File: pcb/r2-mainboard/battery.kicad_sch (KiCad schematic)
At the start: 38 parts, among them J1 USB-C 16P, J2 Pico-Lock 504050-0391, J25 SolderPads 3x, U1 BQ25892RTW, U2 MAX17048G+T10, U3 USBLC6-2SC6

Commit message: R2: the six approved edits, and one of them was already done
Owner-approved 2026-08-19, KiCad closed for the pass.

1. R225 22k -> 20.5K/1%, LCSC C57105 (0402WGF2052TCE, UNI-ROYAL, the
   family the rest of the board already uses). Rendered and checked:
   R224 390k over R225 20.5k with R213 100k injecting VGH_DAC, so
   20.5||100 = 17.01k and VGH = 1.2 x (1 + 390/17.01) = 28.71 V at
   DAC = 0 -- exactly epd-port.md 10.3's target.
2. The five sense-divider caps that carried codes for the wrong
   capacitance -> C1523 (0402B102K500NT, 1 nF 50 V X7R, JLC Basic,
   5.3 M stock). One part covers both the 25 V and 50 V positions.
2b. R88/R224 -> C54920667 (HRC0402F3903DNTO, 390k 1%, 20 k stock).
   C25782 had 14 units against two per board. The owner found this one;
   both obvious alternatives were traps -- C23150 is 0603, and C44937
   is 3.9 ohm despite "390K" in its part number.
3. C147 set DNP rather than deleted. panel.md 7 had already ruled that
   J6.7/J6.44 stay; that covered the pins but not the capacitor on the
   dead net. DNP drops it from placement, keeps the topology of a frozen
   sheet untouched, and leaves the footprint if a future panel drives
   the rail. in_bom stays yes -- that is this board's convention for all
   13 DNP parts, so they show up flagged rather than vanishing.
4. Ten duplicate #PWR references renumbered to #PWR1112-1121 on the
   battery sheet, which was the colliding side in every case.
5. J3 was already deleted on 2026-08-15. No work needed.
6. Specter -> Reflow across 22 files: 14 sheets, 7 generators, the
   project file. .history/ deliberately untouched.

Verified as one change: netlist before and after has 518 nets with
identical pin membership, and epd_power and epd were rendered to PNG and
inspected.

Docs updated to match: epd-port.md 10 is applied rather than designed,
frontlight.md 1 loses the "9 in series is inferred" hedge (the vendor
listing confirms 2 x 9), and io-expansion.md 4's "only guess on this
sheet" is resolved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
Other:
- title: Glider-R2 / Specter mainboard -> Glider-R2 / Reflow mainboard
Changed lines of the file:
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@@
 	(paper "A3")
 	(title_block
-		(title "Glider-R2 / Specter mainboard")
+		(title "Glider-R2 / Reflow mainboard")
 		(date "2026-08-05")
 		(rev "A")
@@
 		(in_pos_files yes)
 		(dnp no)
-		(property "Reference" "#PWR012"
+		(property "Reference" "#PWR1112"
 			(at 236.22 135.89 0)
 			(hide yes)
@@
 			(project "r2"
 				(path "/dee825bf-c2f1-415d-afdf-cf702072a6e8/a6dcf48c-d5d2-42bd-8aa1-b0910921d2ee"
-					(reference "#PWR012")
+					(reference "#PWR1112")
 					(unit 1)
 				)
@@
 		(in_pos_files yes)
 		(dnp no)
-		(property "Reference" "#PWR017"
+		(property "Reference" "#PWR1113"
 			(at 214.63 151.13 0)
 			(hide yes)
@@
 			(project "r2"
 				(path "/dee825bf-c2f1-415d-afdf-cf702072a6e8/a6dcf48c-d5d2-42bd-8aa1-b0910921d2ee"
-					(reference "#PWR017")
+					(reference "#PWR1113")
 					(unit 1)
 				)
@@
 		(in_pos_files yes)
 		(dnp no)
-		(property "Reference" "#PWR022"
+		(property "Reference" "#PWR1115"
 			(at 355.6 101.6 0)
 			(hide yes)
@@
 			(project "r2"
 				(path "/dee825bf-c2f1-415d-afdf-cf702072a6e8/a6dcf48c-d5d2-42bd-8aa1-b0910921d2ee"
-					(reference "#PWR022")
+					(reference "#PWR1115")
 					(unit 1)
 				)
@@
 		(in_pos_files yes)
 		(dnp no)
-		(property "Reference" "#PWR020"
+		(property "Reference" "#PWR1114"
 			(at 271.78 87.63 0)
 			(hide yes)
@@
 			(project "r2"
 				(path "/dee825bf-c2f1-415d-afdf-cf702072a6e8/a6dcf48c-d5d2-42bd-8aa1-b0910921d2ee"
-					(reference "#PWR020")
+					(reference "#PWR1114")
 					(unit 1)
 				)
@@
 		(in_pos_files yes)
 		(dnp no)
-		(property "Reference" "#PWR037"
+		(property "Reference" "#PWR1120"
 			(at 50.8 227.33 0)
 			(hide yes)
@@
 			(project "r2"
 				(path "/dee825bf-c2f1-415d-afdf-cf702072a6e8/a6dcf48c-d5d2-42bd-8aa1-b0910921d2ee"
-					(reference "#PWR037")
+					(reference "#PWR1120")
 					(unit 1)
 				)
@@
 		(in_pos_files yes)
 		(dnp no)
-		(property "Reference" "#PWR025"
+		(property "Reference" "#PWR1116"
 			(at 355.6 140.97 0)
 			(hide yes)
@@
 			(project "r2"
 				(path "/dee825bf-c2f1-415d-afdf-cf702072a6e8/a6dcf48c-d5d2-42bd-8aa1-b0910921d2ee"
-					(reference "#PWR025")
+					(reference "#PWR1116")
 					(unit 1)
 				)
@@
 		(in_pos_files yes)
 		(dnp no)
-		(property "Reference" "#PWR040"
+		(property "Reference" "#PWR1121"
 			(at 292.1 212.09 0)
 			(hide yes)
@@
 			(project "r2"
 				(path "/dee825bf-c2f1-415d-afdf-cf702072a6e8/a6dcf48c-d5d2-42bd-8aa1-b0910921d2ee"
-					(reference "#PWR040")
+					(reference "#PWR1121")
 					(unit 1)
 				)
@@
 		(in_pos_files yes)
 		(dnp no)
-		(property "Reference" "#PWR034"
+		(property "Reference" "#PWR1117"
 			(at 182.88 179.07 0)
 			(hide yes)
@@
 			(project "r2"
 				(path "/dee825bf-c2f1-415d-afdf-cf702072a6e8/a6dcf48c-d5d2-42bd-8aa1-b0910921d2ee"
-					(reference "#PWR034")
+					(reference "#PWR1117")
 					(unit 1)
 				)
@@
 		(in_pos_files yes)
 		(dnp no)
-		(property "Reference" "#PWR035"
+		(property "Reference" "#PWR1118"
 			(at 182.88 208.28 0)
 			(hide yes)
@@
 			(project "r2"
 				(path "/dee825bf-c2f1-415d-afdf-cf702072a6e8/a6dcf48c-d5d2-42bd-8aa1-b0910921d2ee"
-					(reference "#PWR035")
+					(reference "#PWR1118")
 					(unit 1)
 				)
@@
 		(in_pos_files yes)
 		(dnp no)
-		(property "Reference" "#PWR036"
+		(property "Reference" "#PWR1119"
 			(at 30.48 227.33 0)
 			(hide yes)
@@
 			(project "r2"
 				(path "/dee825bf-c2f1-415d-afdf-cf702072a6e8/a6dcf48c-d5d2-42bd-8aa1-b0910921d2ee"
-					(reference "#PWR036")
+					(reference "#PWR1119")
 					(unit 1)
 				)

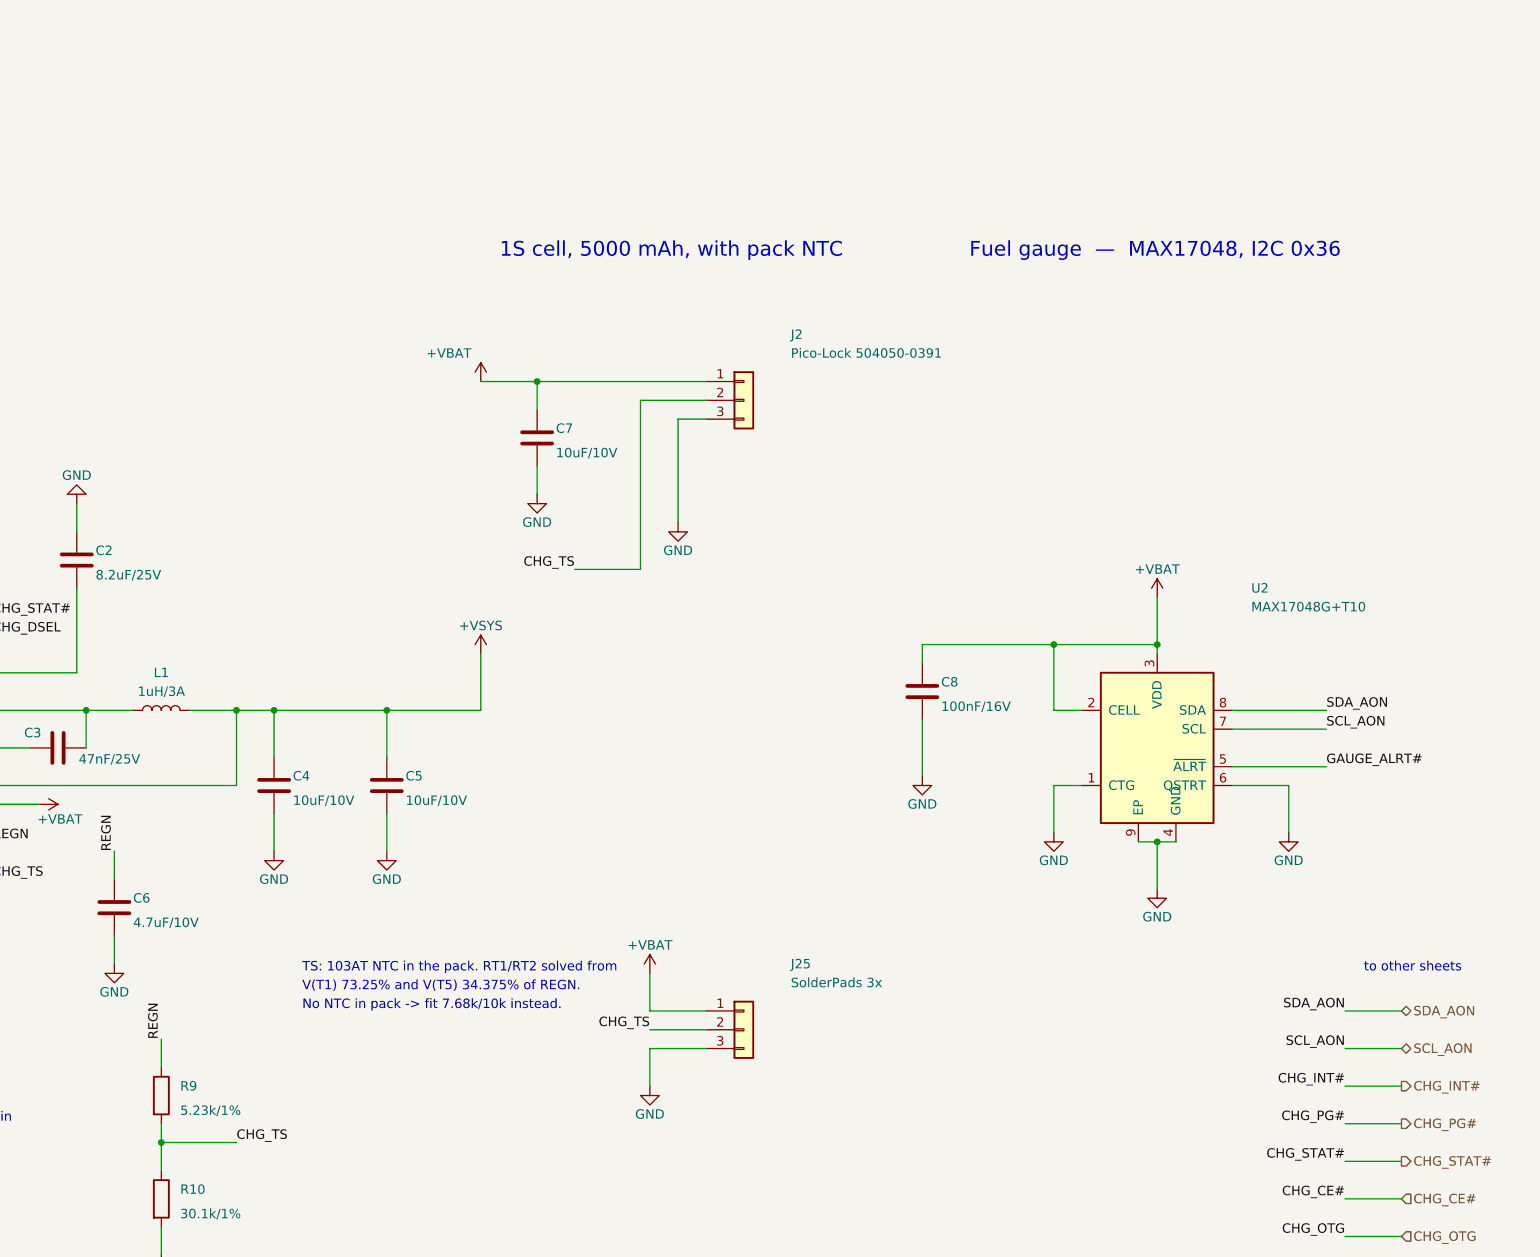
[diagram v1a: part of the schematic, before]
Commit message: R2: C6 goes 0805/10V -> 0603/16V, and clears two DRC errors doing it
The question was whether the REGN decoupling cap could be smaller. It can,
and the smaller part is the better part -- but not for the reason the doc
gave.

bq25896.pdf pin 22 asks for "a 4.7 uF (10 V rating) ceramic capacitor",
placed close to the IC, and gives no range around it -- unlike tps63802.pdf
which publishes a 10-50 uF window for its output cap. So the value is fixed
and the package is the only free variable. REGN sits at 4.7-4.8 V here (spec
table, V(VBUS) = 5 V), and a ceramic loses capacitance with the field across
its dielectric, so a higher rating in a smaller case can beat a lower rating
in a larger one.

Fitted: LCSC C19666, Samsung CL10A475KO8NNNC, 4.7 uF 16 V X5R 0603, a JLCPCB
basic part with 6.35 M in stock. It keeps TI's value, exceeds TI's rating,
and is smaller and lower-ESL than the 0805 -- which serves bq25896.pdf
section 12.1 guideline 6 better than the part it replaces. 0402 was rejected:
the cheap one is +-20 % before derating at 2.1x voltage margin, and the 25 V
one costs 4x a basic part to save 0.7 mm2.

DRC went 46 -> 44. The 0805's pad 2 sat 0.075 mm from a Net-(C3-Pad2) track
against the PWR netclass's 0.110 mm; 0603 pulls it back 0.175 mm and clears
both violations. Unconnected unchanged at 499, ERC unchanged at 32.

battery.md section 6 is corrected while here. It claimed the TS divider's
loading is why 4.7 uF is not optional. It is not -- that divider draws 377 uA
of steady DC, which constrains the LDO, not the capacitor. The reasons are
pin 22 and the gate drive. Ripple was checked and is not binding either: even
at a generous 20 nC per cycle, 1 uF effective gives 0.42 % of REGN against
1-1.4 % TS hysteresis bands.

C6 also gained the check_pcb.py proximity rule it never had, 5.0 mm to U1,
the same limit as its neighbours C1/C2/C3. It sits at 4.15 mm and passes.

Note: r2.kicad_pcb and r2.kicad_pro in this commit also carry the owner's
uncommitted placement wor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
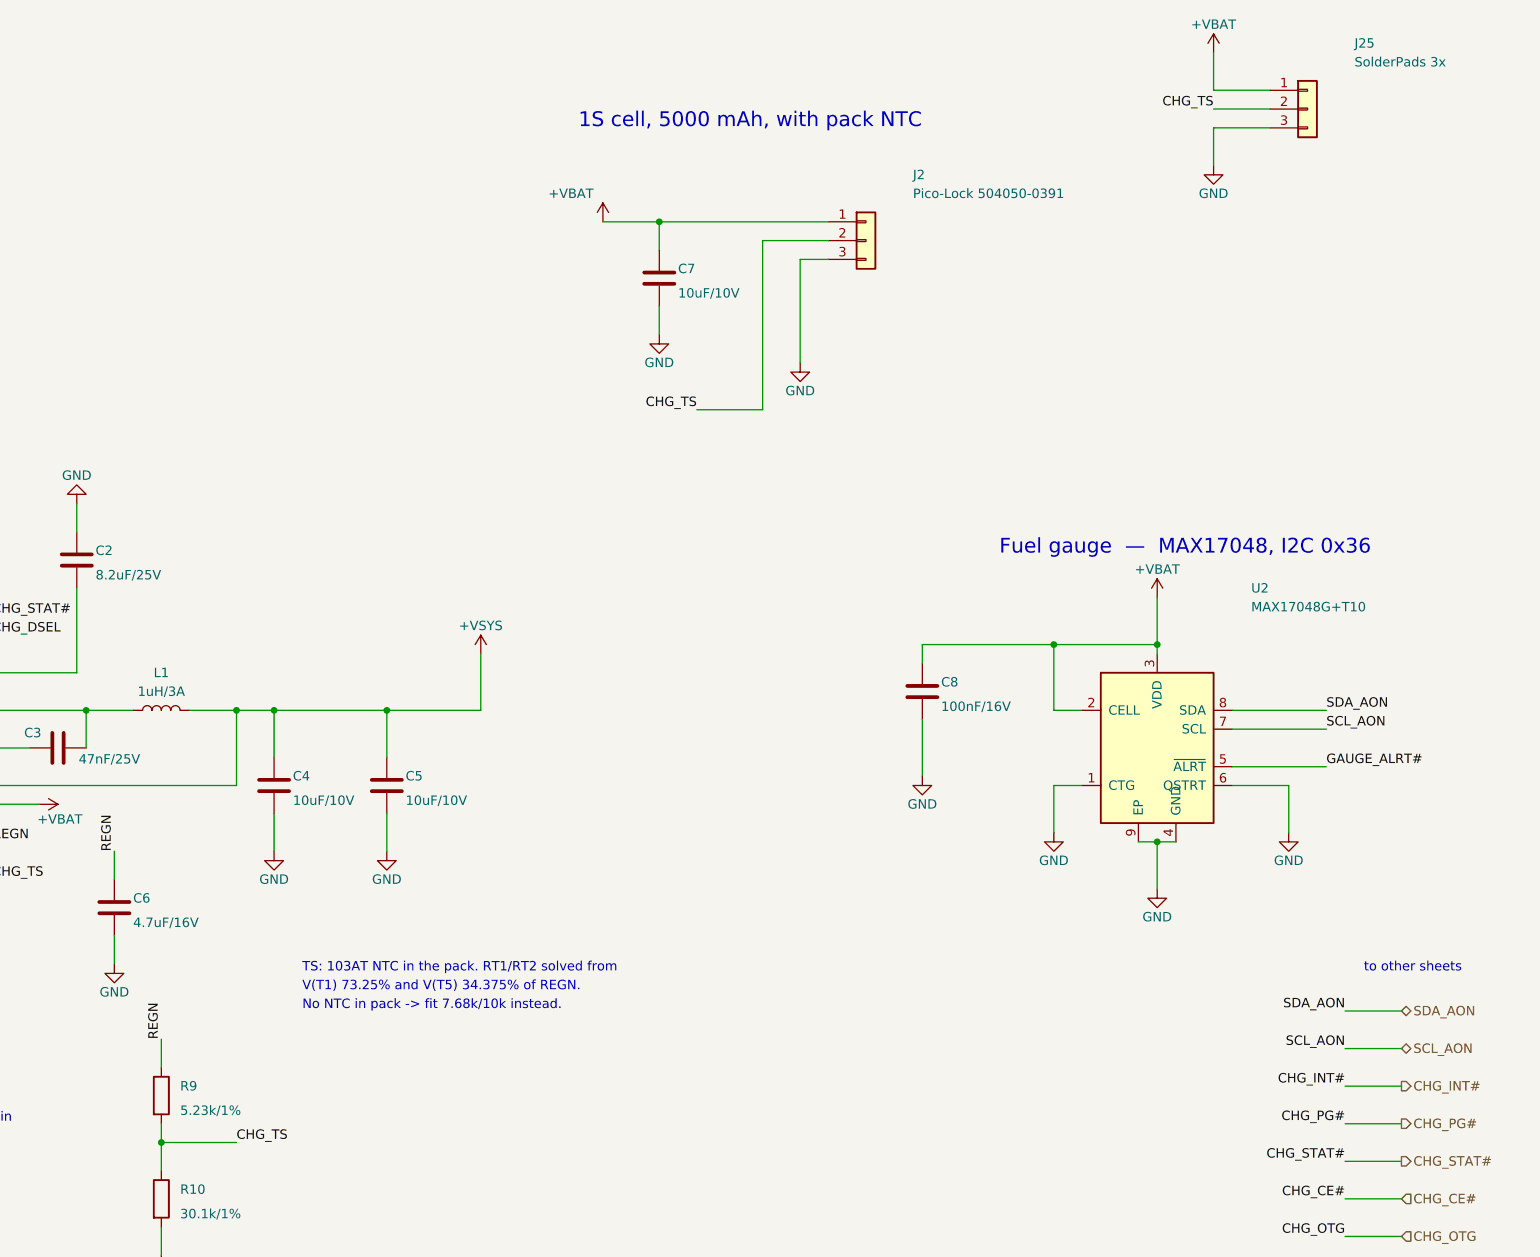
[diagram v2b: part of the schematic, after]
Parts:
- C6: value 4.7uF/10V -> 4.7uF/16V; footprint Capacitor_SMD:C_0805_2012Metric -> Capacitor_SMD:C_0603_1608Metric
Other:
- moved on the sheet: C7, J2, J25

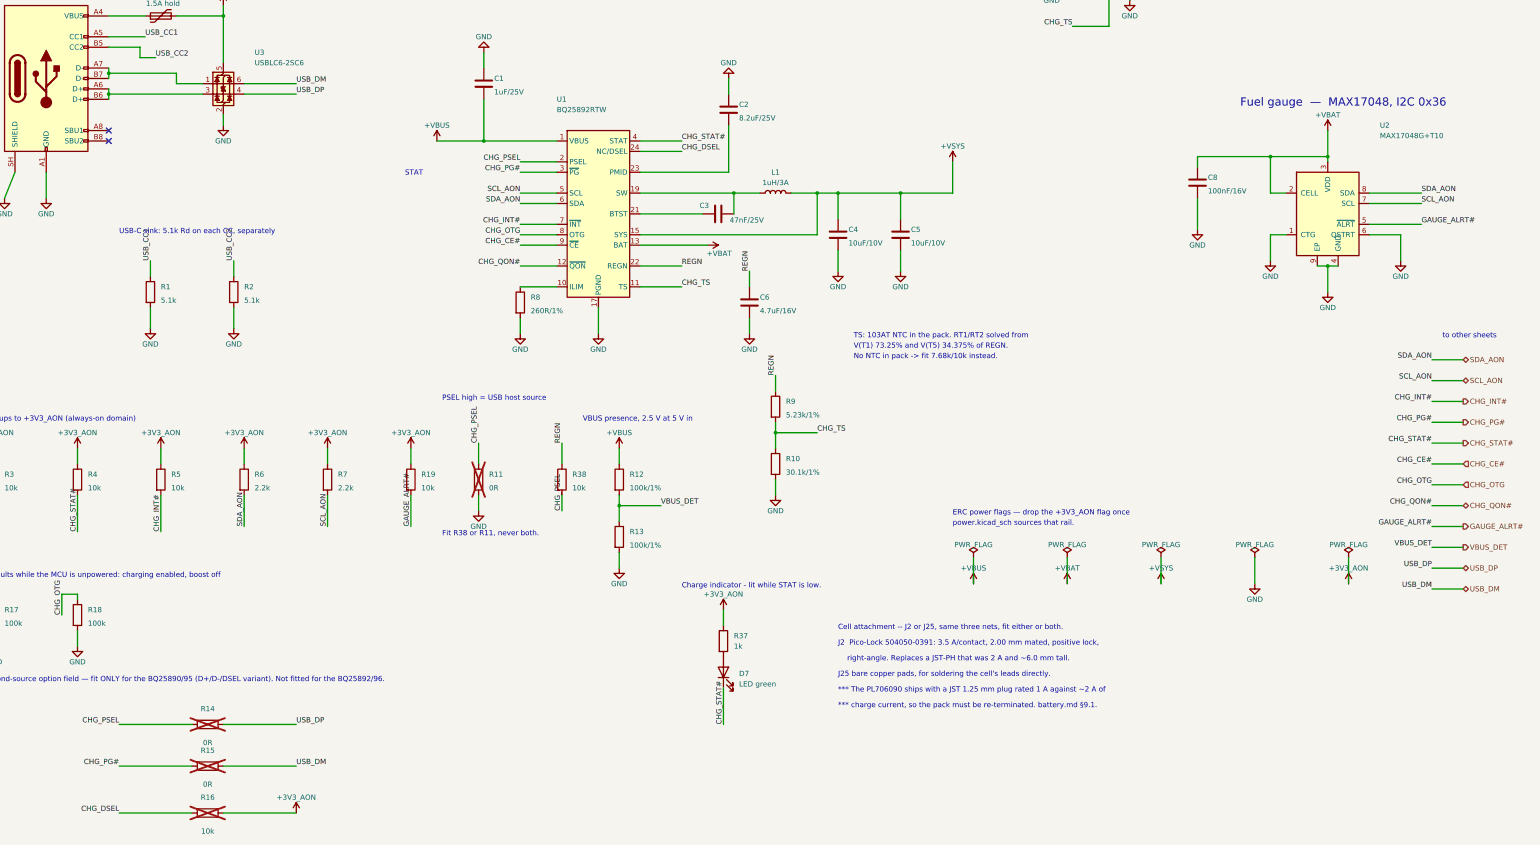
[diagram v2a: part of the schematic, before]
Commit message: R2: withdraw the RWU0007A thermal-pad concern -- it was wrong
power.md §7 item 2 said KiCad's Texas_RWU0007A_VQFN-7_2x2mm_P0.5mm leaves the
thermal-pad segments unnumbered, so U12's heat path is not tied to GND, and to
copy the footprint into r2.pretty and renumber those pads 1 before layout.

Reading the placed footprint with the layer field visible: the six unnumbered
pads are F.Paste ONLY. They are stencil apertures -- each large pad split into
two openings to control solder volume, the standard idiom at that size. Pads
1/2/3 are F.Cu + F.Mask, numbered, and netted GND / SW / +5V_DCDC. Pin 1 is the
thermal path per Table 5-1 and it is on GND already.

Acting on the note would have renumbered paste apertures into copper and
shorted GND, SW and VOUT together -- creating the failure it was meant to
prevent. Found because the owner is routing U12 right now.

§11.2 item 5 amended to a plain layout instruction, and §8's open-items list
no longer carries it.

Co-Authored-By: Claude Opus 5 <noreply@anthropic.com>
Claude-Session: https://claude.ai/code/session_01MnesETWABbVdbcVnCKfKVs
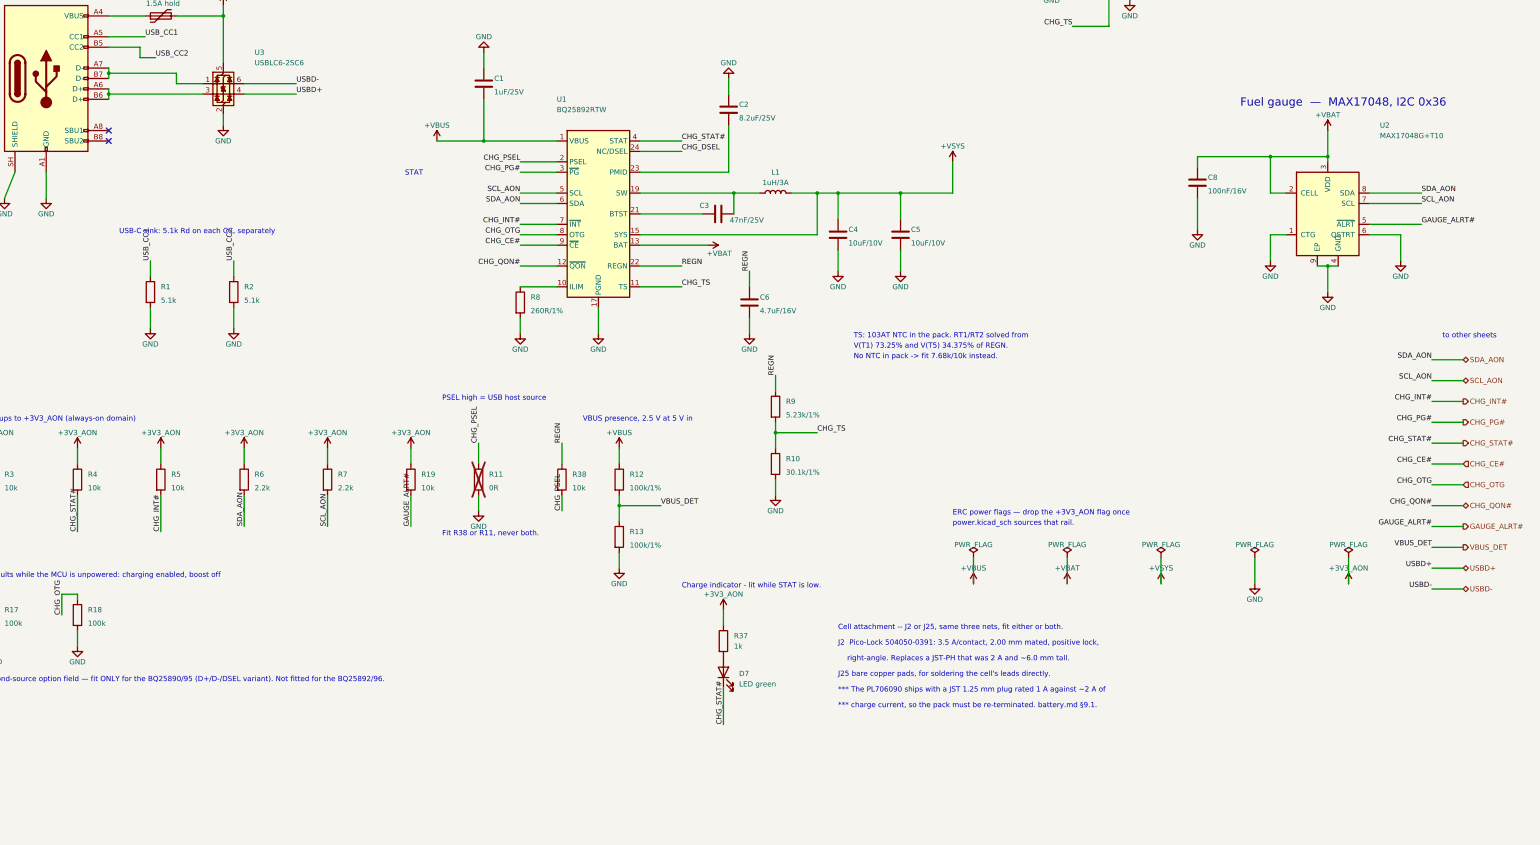
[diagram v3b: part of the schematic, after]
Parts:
- removed R14, R15: 0R, Resistor_SMD:R_0402_1005Metric, symbol Device:R
- removed R16: 10k, Resistor_SMD:R_0402_1005Metric, symbol Device:R
- C4, C5, C7: footprint Capacitor_SMD:C_0805_2012Metric -> Capacitor_SMD:C_0402_1005Metric
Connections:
- net USB_DM renamed USBD-
- net USB_DP renamed USBD+
